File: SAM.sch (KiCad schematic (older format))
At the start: 26 parts

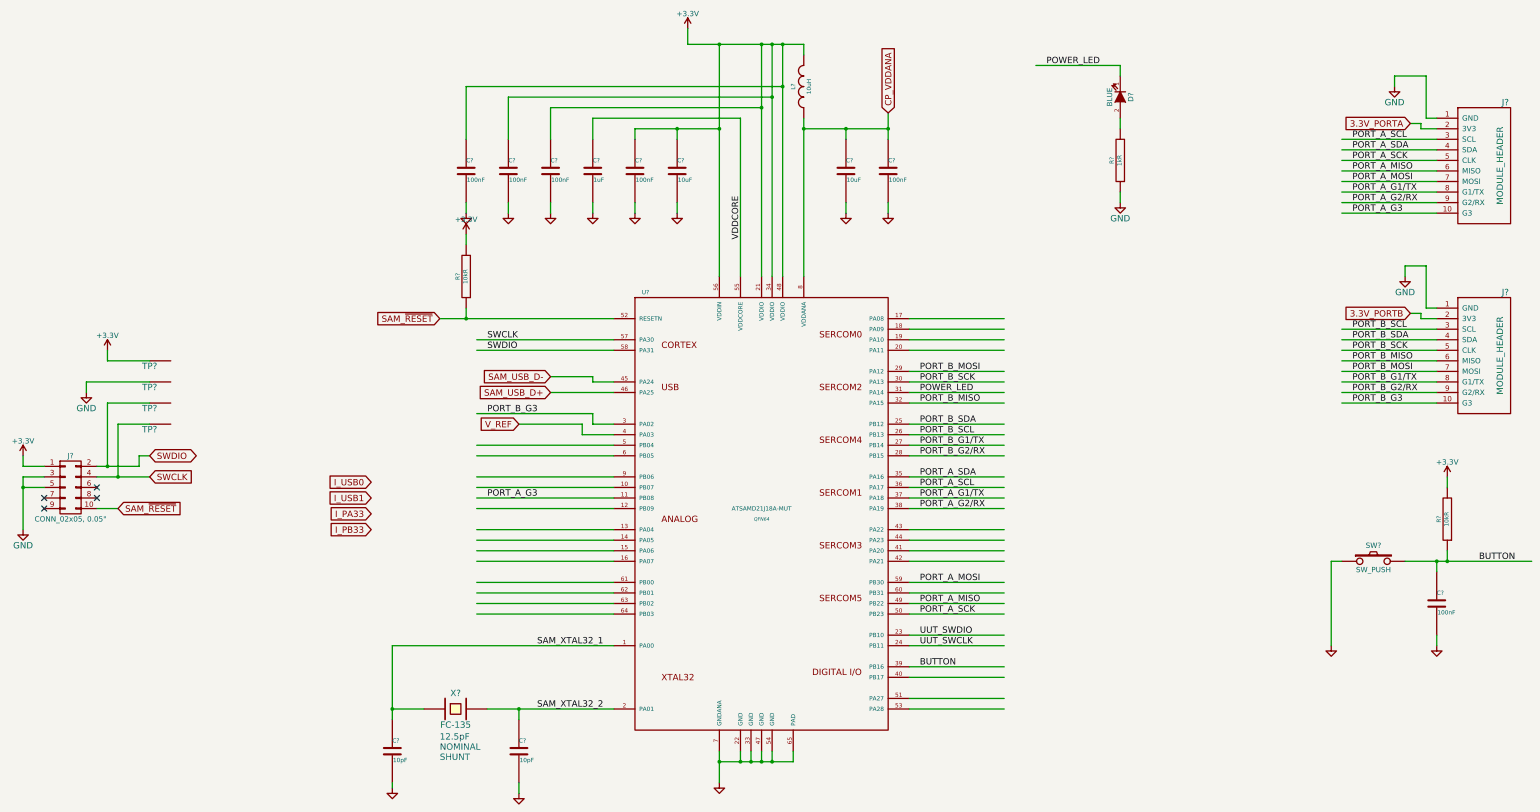
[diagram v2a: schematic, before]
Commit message: pin allocations and finally got the opamp in there
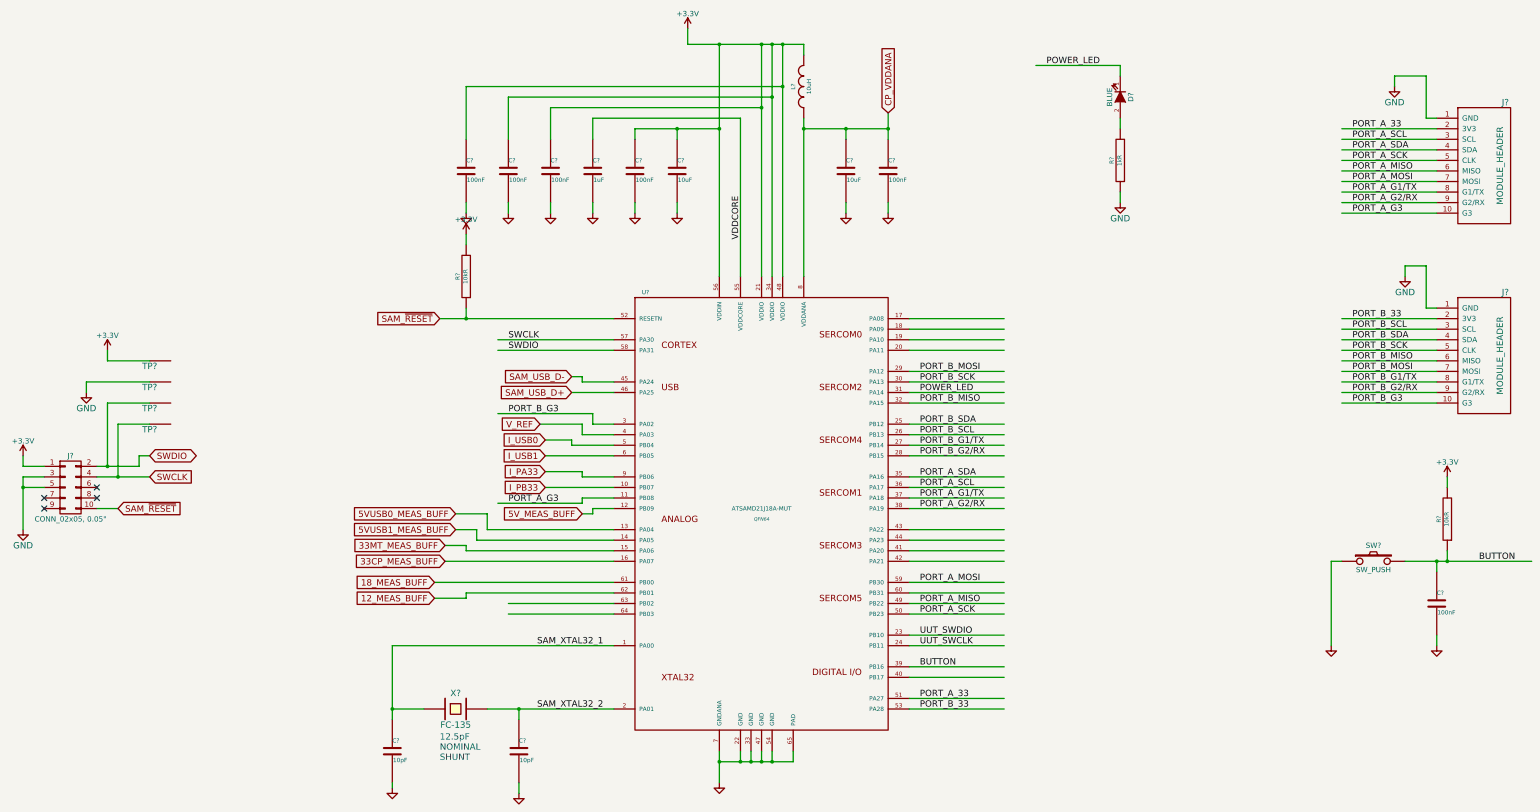
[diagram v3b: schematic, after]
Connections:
- net labels added: 12_MEAS_BUFF, 18_MEAS_BUFF, 33CP_MEAS_BUFF, 33MT_MEAS_BUFF, 5VUSB0_MEAS_BUFF, 5VUSB1_MEAS_BUFF, 5V_MEAS_BUFF, PORT_A_33, PORT_B_33
- net labels removed: 3.3V_PORTA, 3.3V_PORTB
- wire segments 188 -> 175
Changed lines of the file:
@@
 Text GLabel 2100 6400 2    60   Input ~ 0
 SAM_~RESET
-Text GLabel 14350 2750 0    60   Input ~ 0
-3.3V_PORTA
 $Comp
 L GND #PWR?
@@
 Text GLabel 5150 4600 0    60   Input ~ 0
 SAM_~RESET
-Text Label 5600 4800 0    60   ~ 0
+Text Label 5800 4800 0    60   ~ 0
 SWCLK
-Text Label 5600 4900 0    60   ~ 0
+Text Label 5800 4900 0    60   ~ 0
 SWDIO
 Text Label 13800 5100 0    60   ~ 0
@@
 Text Label 9700 5900 0    60   ~ 0
 PORT_B_G2/RX
-Text Label 5600 5500 0    60   ~ 0
+Text Label 5800 5500 0    60   ~ 0
 PORT_B_G3
 Text Label 9700 7100 0    60   ~ 0
@@
 Text Label 9700 6400 0    60   ~ 0
 PORT_A_G2/RX
-Text Label 5600 6300 0    60   ~ 0
+Text Label 5800 6350 0    60   ~ 0
 PORT_A_G3
 $Comp
@@
 	1    0    0    -1
 $EndComp
-Text GLabel 14350 4550 0    60   Input ~ 0
-3.3V_PORTB
 Text Label 9700 7900 0    60   ~ 0
 BUTTON
-Text GLabel 6200 5300 0    60   Input ~ 0
+Text GLabel 6400 5300 0    60   Input ~ 0
 SAM_USB_D+
-Text GLabel 6200 5150 0    60   Input ~ 0
+Text GLabel 6400 5150 0    60   Input ~ 0
 SAM_USB_D-
-Text GLabel 5900 5600 0    60   Input ~ 0
+Text GLabel 6100 5600 0    60   Input ~ 0
 V_REF
 Text Label 9700 7600 0    60   ~ 0
@@
 $EndComp
 Wire Wire Line
-	6200 5300 6800 5300
-Wire Wire Line
-	6600 5150 6200 5150
-Wire Wire Line
-	6600 5200 6600 5150
+	6400 5300 6800 5300
+Wire Wire Line
+	6500 5150 6400 5150
+Wire Wire Line
+	6500 5200 6500 5150
 Wire Wire Line
 	13700 3000 14600 3000
@@
 Connection ~ 7800 2000
 Wire Wire Line
-	7800 2000 7800 2800
-Wire Wire Line
-	7800 2800 7800 4200
+	7800 2000 7800 4200
 Connection ~ 8200 2600
 Connection ~ 8200 2000
@@
 Connection ~ 8300 2000
 Wire Wire Line
-	8300 2000 8300 2500
-Wire Wire Line
-	8300 2500 8300 4200
+	8300 2000 8300 4200
 Wire Wire Line
 	7500 2000 7500 1850
@@
 	8200 2600 6200 2600
 Wire Wire Line
-	8200 2000 8200 2600
-Wire Wire Line
-	8200 2600 8200 4200
+	8200 2000 8200 4200
 Wire Wire Line
 	8000 2700 8000 4200
@@
 	7000 2800 7000 2900
 Wire Wire Line
-	7000 2800 7400 2800
-Wire Wire Line
-	7400 2800 7800 2800
+	7000 2800 7800 2800
 Connection ~ 8600 2800
 Connection ~ 9000 2800
 Wire Wire Line
-	9400 2650 9400 2800
-Wire Wire Line
-	9400 2800 9400 2900
+	9400 2650 9400 2900
 Wire Wire Line
 	9000 2800 9000 2900
 Wire Wire Line
-	8600 2800 9000 2800
-Wire Wire Line
-	9000 2800 9400 2800
-Wire Wire Line
-	8600 2700 8600 2800
-Wire Wire Line
-	8600 2800 8600 4200
+	8600 2800 9400 2800
+Wire Wire Line
+	8600 2700 8600 4200
 Wire Wire Line
 	4700 9000 4700 9050
@@
 	4700 8300 5000 8300
 Wire Wire Line
-	4700 7700 4700 8300
-Wire Wire Line
-	4700 8300 4700 8400
+	4700 7700 4700 8400
 Wire Wire Line
 	9600 7100 10500 7100
@@
 	9600 5100 10500 5100
 Wire Wire Line
-	5600 8300 5900 8300
-Wire Wire Line
-	5900 8300 6800 8300
+	5600 8300 6800 8300
 Wire Wire Line
 	4700 7700 6800 7700
@@
 	9600 7900 10500 7900
 Wire Wire Line
-	6800 5200 6600 5200
-Wire Wire Line
-	6800 4900 5500 4900
-Wire Wire Line
-	6800 4800 5500 4800
-Wire Wire Line
-	5150 4600 5400 4600
-Wire Wire Line
-	5400 4600 6800 4600
-Wire Wire Line
-	7500 2000 7800 2000
-Wire Wire Line
-	7800 2000 8200 2000
-Wire Wire Line
-	8200 2000 8300 2000
-Wire Wire Line
-	8300 2000 8400 2000
-Wire Wire Line
-	8400 2000 8600 2000
+	6800 5200 6500 5200
+Wire Wire Line
+	6800 4900 5700 4900
+Wire Wire Line
+	6800 4800 5700 4800
+Wire Wire Line
+	5150 4600 6800 4600
+Wire Wire Line
+	7500 2000 8600 2000
 Wire Wire Line
 	7400 2900 7400 2800
 Connection ~ 7400 2800
 Wire Wire Line
-	7800 8700 7800 8800
-Wire Wire Line
-	7800 8800 7800 9000
-Wire Wire Line
-	7800 8800 8000 8800
-Wire Wire Line
-	8000 8800 8100 8800
-Wire Wire Line
-	8100 8800 8200 8800
-Wire Wire Line
-	8200 8800 8300 8800
-Wire Wire Line
-	8300 8800 8500 8800
+	7800 8700 7800 9000
+Wire Wire Line
+	7800 8800 8500 8800
 Wire Wire Line
 	8000 8800 8000 8700
@@
 	14700 6100 14700 6200
 Wire Wire Line
-	14300 6900 14600 6900
-Wire Wire Line
-	14600 6900 14700 6900
-Wire Wire Line
-	14700 6900 15500 6900
+	14300 6900 15500 6900
 Wire Wire Line
 	14700 6900 14700 6800
@@
 	1400 6200 1200 6200
 Wire Wire Line
-	1200 6100 1200 6200
-Wire Wire Line
-	1200 6200 1200 6600
+	1200 6100 1200 6600
 Wire Wire Line
 	1400 6100 1200 6100
@@
 	2100 6400 1900 6400
 Wire Wire Line
-	1900 6100 2100 6100
-Wire Wire Line
-	2100 6100 2400 6100
-Wire Wire Line
-	1900 6000 2000 6000
-Wire Wire Line
-	2000 6000 2300 6000
+	1900 6100 2400 6100
+Wire Wire Line
+	1900 6000 2300 6000
 Wire Wire Line
 	1200 6000 1200 5900
@@
 	2300 5900 2400 5900
 Wire Wire Line
-	14600 2800 14450 2800
-Wire Wire Line
-	14450 4600 14600 4600
+	14600 2800 13700 2800
+Wire Wire Line
+	13700 4600 14600 4600
 Wire Wire Line
 	14600 3100 13700 3100
@@
 	14500 2700 14600 2700
 Wire Wire Line
-	14450 4600 14450 4550
-Wire Wire Line
-	14450 4550 14350 4550
-Wire Wire Line
-	14450 2800 14450 2750
-Wire Wire Line
-	14450 2750 14350 2750
-Wire Wire Line
 	14500 2700 14500 2300
 Wire Wire Line
@@
 	11600 2200 10800 2200
 Wire Wire Line
-	5500 5500 6600 5500
+	5700 5500 6600 5500
 Wire Wire Line
 	6600 5500 6600 5600
@@
 	6500 5700 6500 5600
 Wire Wire Line
-	6500 5600 5900 5600
+	6500 5600 6100 5600
 Wire Wire Line
 	5400 3600 5400 3500
@@
 	5400 2400 8400 2400
 Wire Wire Line
-	8400 2000 8400 2400
-Wire Wire Line
-	8400 2400 8400 4200
+	8400 2000 8400 4200
 Connection ~ 8400 2000
 Connection ~ 8400 2400
@@
 Connection ~ 8300 8800
 Wire Wire Line
-	6800 5800 5500 5800
-Wire Wire Line
-	6800 5900 5500 5900
-Wire Wire Line
-	6800 6100 5500 6100
-Wire Wire Line
-	6800 6200 5500 6200
-Wire Wire Line
-	6800 6300 5500 6300
-Wire Wire Line
-	6800 6400 5500 6400
-Wire Wire Line
-	6800 6600 5500 6600
-Wire Wire Line
-	6800 6700 5500 6700
-Wire Wire Line
-	6800 6800 5500 6800
-Wire Wire Line
-	6800 6900 5500 6900
-Wire Wire Line
-	6800 7100 5500 7100
-Wire Wire Line
-	6800 7200 5500 7200
-Wire Wire Line
-	6800 7300 5500 7300
-Wire Wire Line
-	6800 7400 5500 7400
-Text GLabel 4500 6150 0    60   Input ~ 0
+	6800 5900 6150 5900
+Wire Wire Line
+	6800 6100 6500 6100
+Wire Wire Line
+	6800 6200 6150 6200
+Wire Wire Line
+	5600 6600 6800 6600
+Wire Wire Line
+	5500 6700 6800 6700
+Wire Wire Line
+	5400 6800 6800 6800
+Wire Wire Line
+	5200 6900 6800 6900
+Wire Wire Line
+	6800 7100 5100 7100
+Wire Wire Line
+	5400 7200 6800 7200
+Wire Wire Line
+	6800 7300 5800 7300
+Wire Wire Line
+	6800 7400 5800 7400
+Text GLabel 6150 5750 0    60   Input ~ 0
 I_USB0
-Text GLabel 4500 6300 0    60   Input ~ 0
+Text GLabel 6150 5900 0    60   Input ~ 0
 I_USB1
-Text GLabel 4500 6450 0    60   Input ~ 0
+Text GLabel 6150 6050 0    60   Input ~ 0
 I_PA33
-Text GLabel 4500 6600 0    60   Input ~ 0
+Text GLabel 6150 6200 0    60   Input ~ 0
 I_PB33
 Wire Wire Line
 	10500 8000 9600 8000
+Text GLabel 6500 6450 0    60   Input ~ 0
+5V_MEAS_BUFF
+Text GLabel 5200 6750 0    60   Input ~ 0
+33MT_MEAS_BUFF
+Text GLabel 5200 6900 0    60   Input ~ 0
+33CP_MEAS_BUFF
+Text GLabel 5100 7100 0    60   Input ~ 0
+18_MEAS_BUFF
+Text GLabel 5100 7250 0    60   Input ~ 0
+12_MEAS_BUFF
+Text GLabel 5300 6450 0    60   Input ~ 0
+5VUSB0_MEAS_BUFF
+Text GLabel 5300 6600 0    60   Input ~ 0
+5VUSB1_MEAS_BUFF
+Text Label 13800 2800 0    60   ~ 0
+PORT_A_33
+Text Label 13800 4600 0    60   ~ 0
+PORT_B_33
+Text Label 9700 8200 0    60   ~ 0
+PORT_A_33
+Text Label 9700 8300 0    60   ~ 0
+PORT_B_33
+Wire Wire Line
+	6800 5800 6400 5800
+Wire Wire Line
+	6400 5800 6400 5750
+Wire Wire Line
+	6400 5750 6150 5750
+Wire Wire Line
+	6500 6100 6500 6050
+Wire Wire Line
+	6500 6050 6150 6050
+Wire Wire Line
+	5700 6350 6500 6350
+Wire Wire Line
+	6500 6350 6500 6300
+Wire Wire Line
+	6500 6300 6800 6300
+Wire Wire Line
+	6800 6400 6600 6400
+Wire Wire Line
+	6600 6400 6600 6450
+Wire Wire Line
+	6600 6450 6500 6450
+Wire Wire Line
+	5600 6600 5600 6450
+Wire Wire Line
+	5600 6450 5300 6450
+Wire Wire Line
+	5300 6600 5500 6600
+Wire Wire Line
+	5500 6600 5500 6700
+Wire Wire Line
+	5400 6800 5400 6750
+Wire Wire Line
+	5400 6750 5200 6750
+Wire Wire Line
+	5400 7200 5400 7250
+Wire Wire Line
+	5400 7250 5100 7250
 $EndSCHEMATC

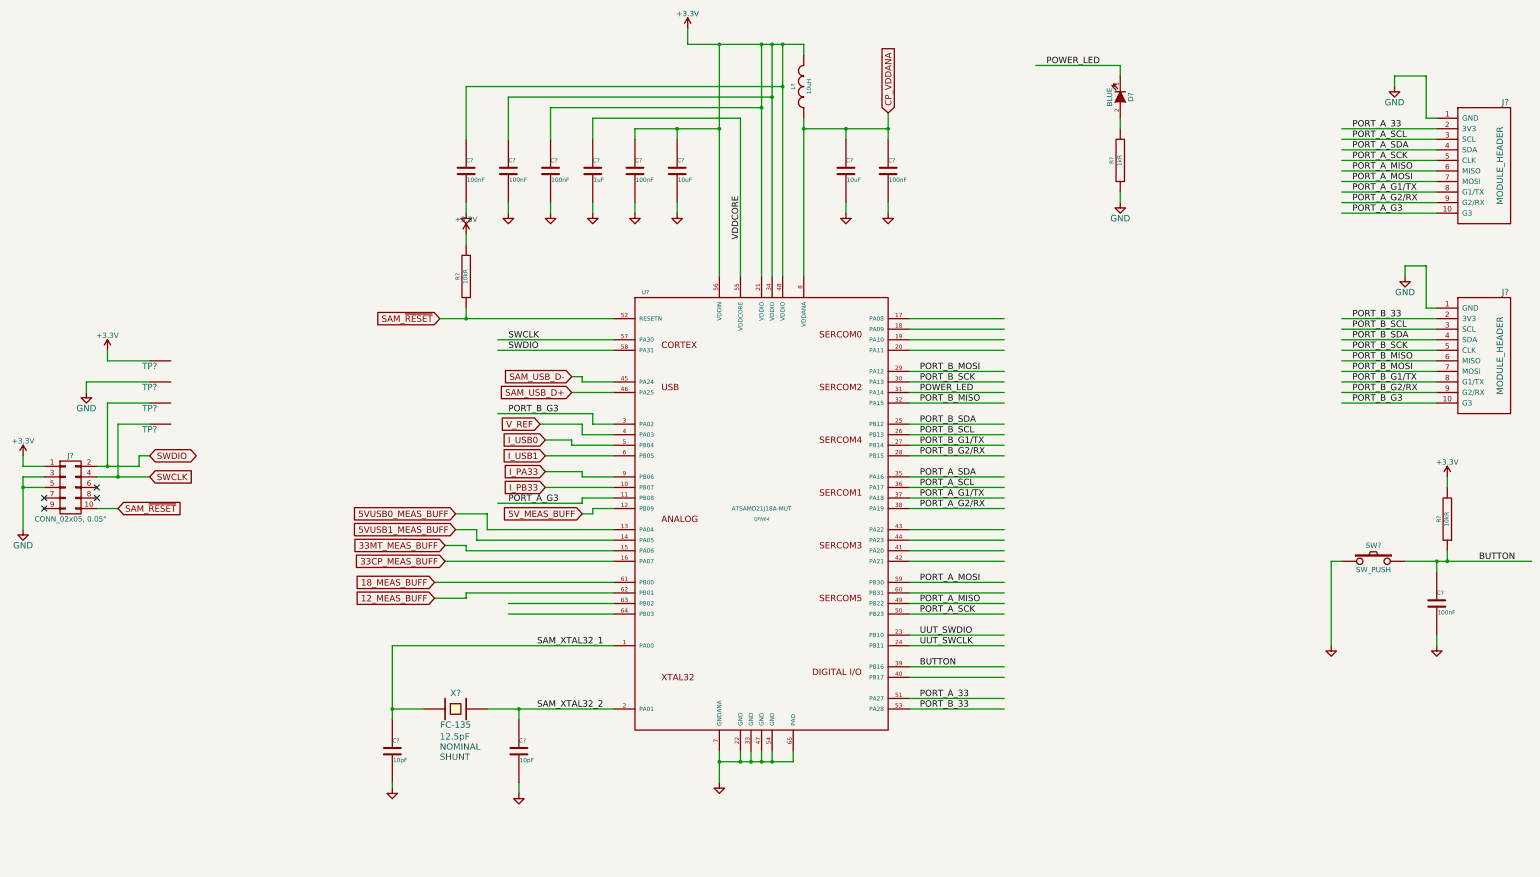
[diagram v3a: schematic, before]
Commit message: connected analog things, lots of testpoints
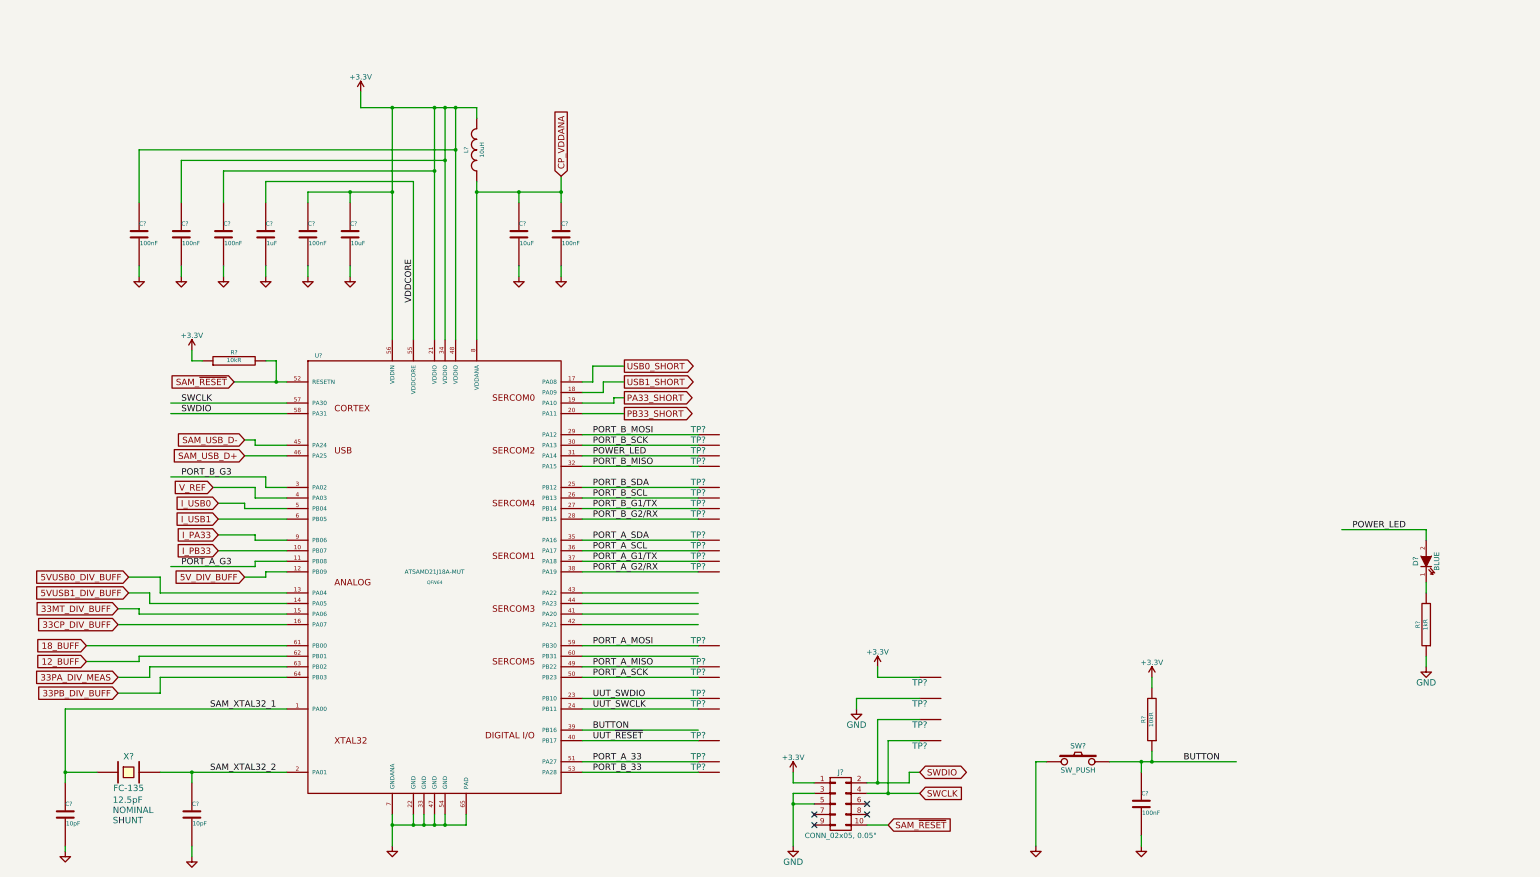
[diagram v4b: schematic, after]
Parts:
- removed J? (x2): MODULE_HEADER, tm-kicad-lib:MODULE_HEADER_TESSEL-backside, symbol MODULE_HEADER
- added TP? (x20): TP, tm-kicad-lib:Testpoint, symbol TP
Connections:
- net labels added: 12_BUFF, 18_BUFF, 33CP_DIV_BUFF, 33MT_DIV_BUFF, 33PA_DIV_MEAS, 33PB_DIV_BUFF, 5VUSB0_DIV_BUFF, 5VUSB1_DIV_BUFF, 5V_DIV_BUFF, PA33_SHORT, PB33_SHORT, USB0_SHORT, USB1_SHORT, UUT_~RESET
- net labels removed: 12_MEAS_BUFF, 18_MEAS_BUFF, 33CP_MEAS_BUFF, 33MT_MEAS_BUFF, 5VUSB0_MEAS_BUFF, 5VUSB1_MEAS_BUFF, 5V_MEAS_BUFF
- wire segments 175 -> 186
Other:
- moved on the sheet: C?, D?, J?, L?, R?, SW?, TP?, U?, X?
